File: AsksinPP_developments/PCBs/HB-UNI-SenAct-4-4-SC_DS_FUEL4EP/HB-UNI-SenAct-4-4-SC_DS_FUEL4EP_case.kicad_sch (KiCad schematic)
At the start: 29 parts, among them J1 5V supply, J3 4x Relais, J4 5x LEDs, J5 4x Push Buttons, J6 Accumulator, SW1 Heating, SW2 Monitor, SW3 Hifiberry, SW4 AC supply

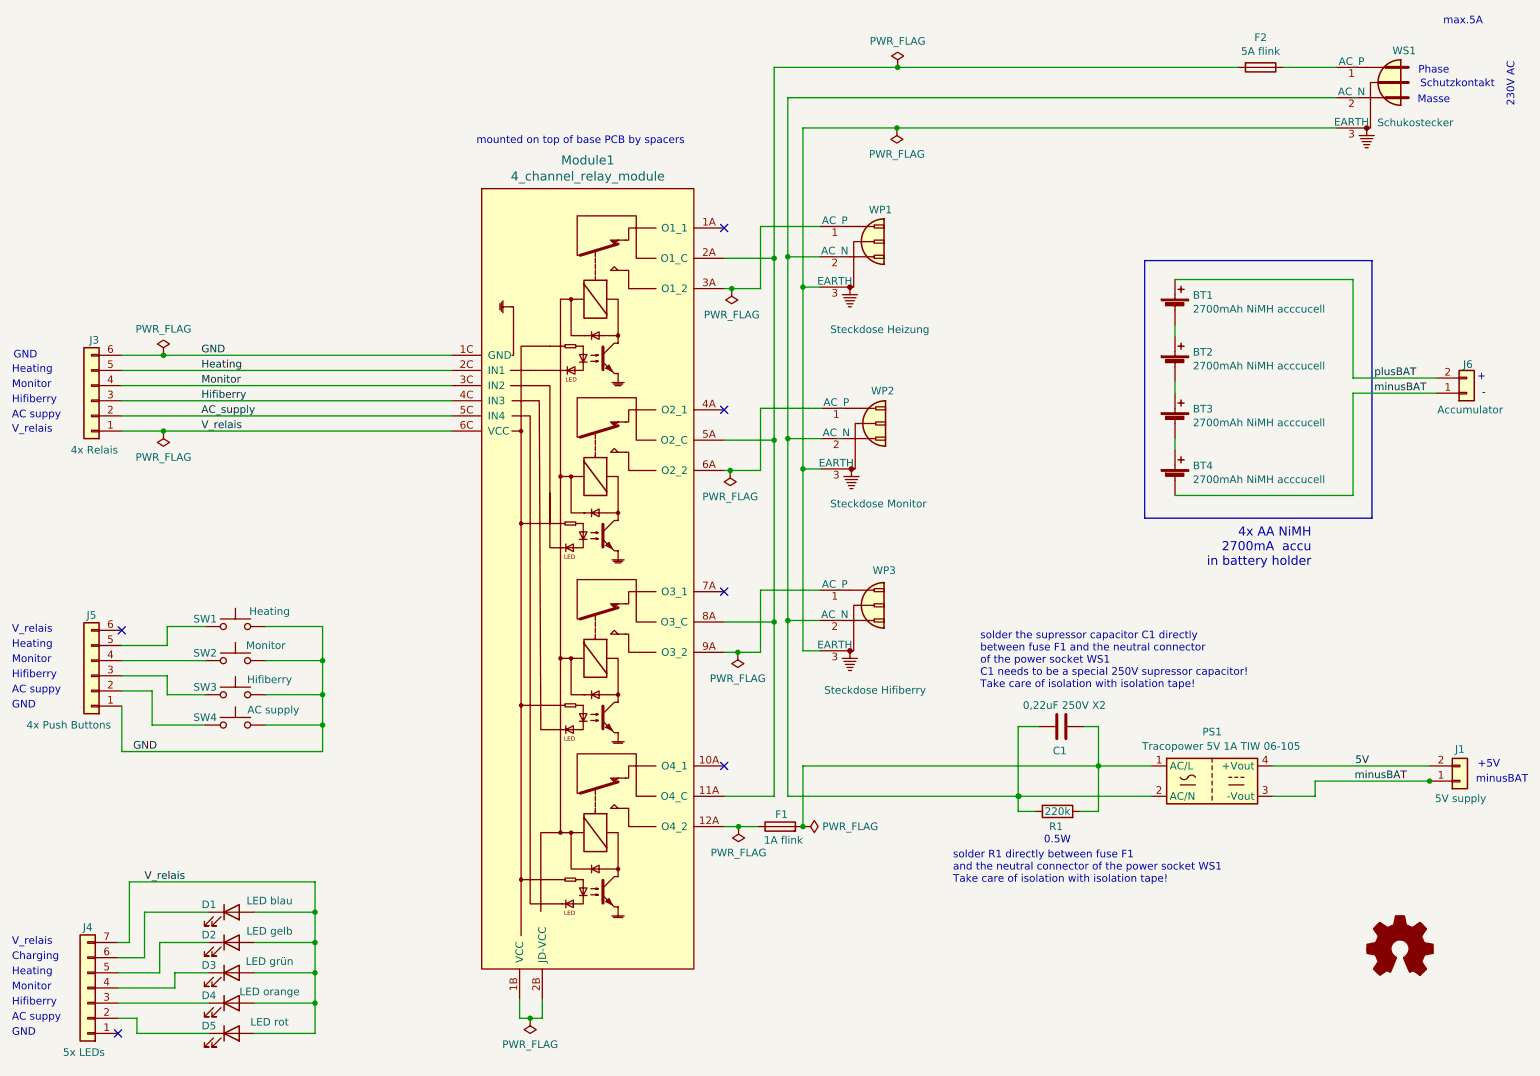
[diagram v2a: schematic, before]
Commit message: PCBs/HB-UNI-SenAct-4-4-SC_DS_FUEL4EP: migration to KiCAD 8
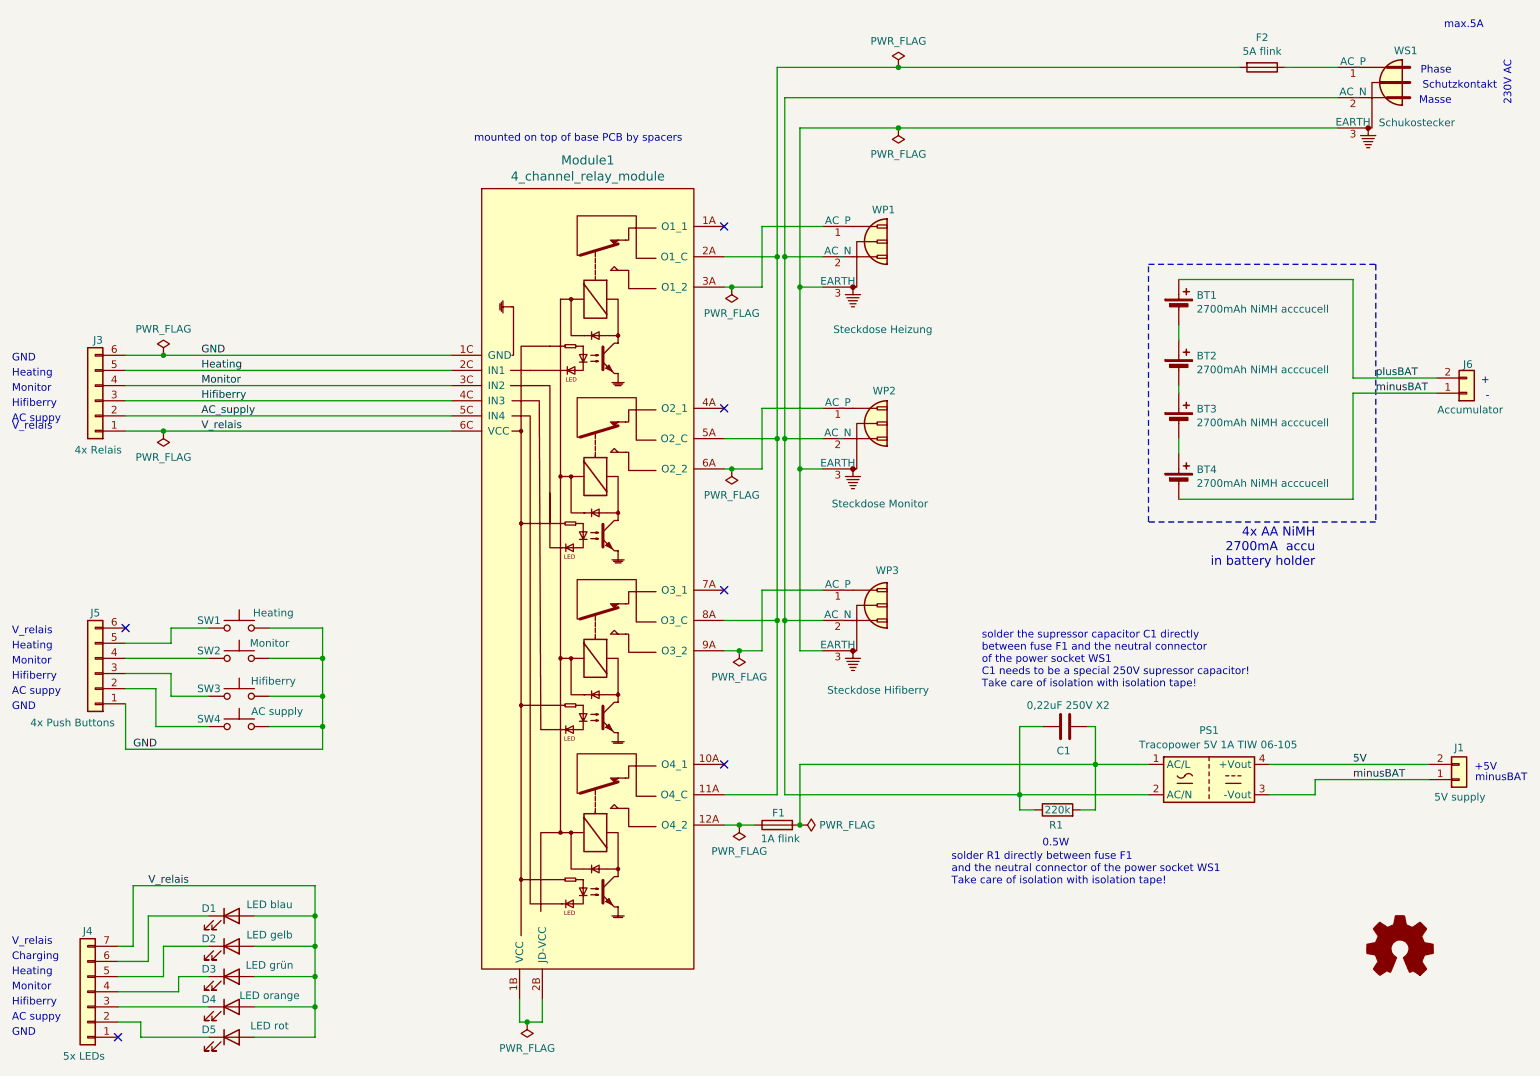
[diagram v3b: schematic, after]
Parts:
- PS1: footprint Converter_ACDC:Converter_ACDC_HiLink_HLK-PMxx -> Converter_ACDC:Converter_ACDC_Hi-Link_HLK-PMxx
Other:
- moved on the sheet: BT1, BT2, BT3, BT4, C1, D1, D2, D3, D4, D5, F1, J3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
